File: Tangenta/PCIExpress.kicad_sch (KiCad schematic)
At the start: 0 parts

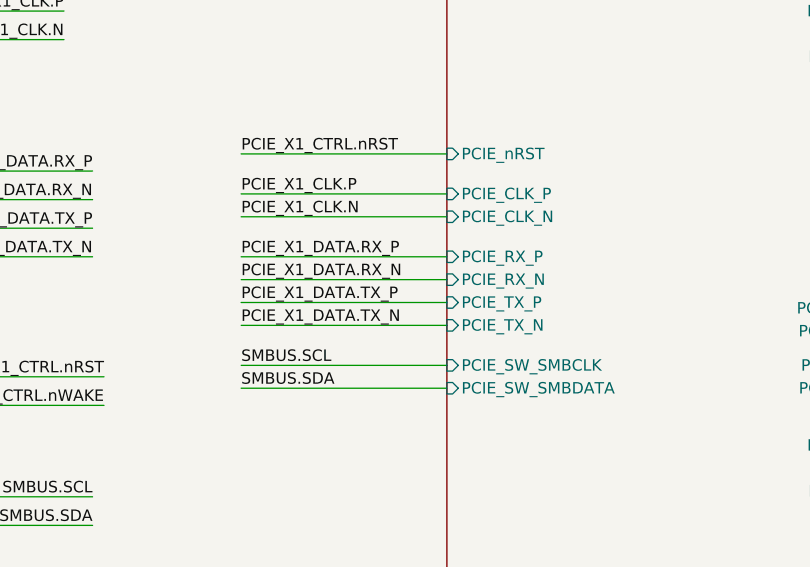
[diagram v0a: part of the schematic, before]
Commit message: PCIe fix in progress...
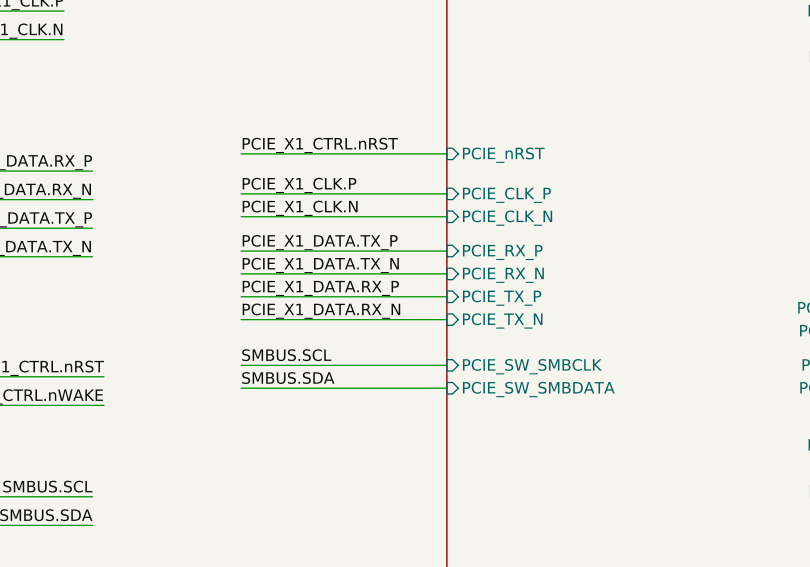
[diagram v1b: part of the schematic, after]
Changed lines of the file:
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@@
 	(wire
 		(pts
-			(xy 101.6 120.015) (xy 124.46 120.015)
+			(xy 101.6 119.38) (xy 124.46 119.38)
 		)
 		(stroke
@@
 	(wire
 		(pts
-			(xy 101.6 117.475) (xy 124.46 117.475)
+			(xy 101.6 116.84) (xy 124.46 116.84)
 		)
 		(stroke
@@
 	(wire
 		(pts
-			(xy 101.6 125.095) (xy 124.46 125.095)
+			(xy 101.6 124.46) (xy 124.46 124.46)
 		)
 		(stroke
@@
 	(wire
 		(pts
-			(xy 101.6 122.555) (xy 124.46 122.555)
+			(xy 101.6 121.92) (xy 124.46 121.92)
 		)
 		(stroke
@@
 	)
 	(label "PCIE_X1_DATA.TX_P"
-		(at 101.6 122.555 0)
+		(at 101.6 116.84 0)
 		(effects
 			(font
@@
 	)
 	(label "PCIE_X1_DATA.TX_N"
-		(at 101.6 125.095 0)
+		(at 101.6 119.38 0)
 		(effects
 			(font
@@
 	)
 	(label "PCIE_X1_DATA.RX_P"
-		(at 101.6 117.475 0)
+		(at 101.6 121.92 0)
 		(effects
 			(font
@@
 	)
 	(label "PCIE_X1_DATA.RX_N"
-		(at 101.6 120.015 0)
+		(at 101.6 124.46 0)
 		(effects
 			(font
@@
 		)
 		(pin "PCIE_RX_P" input
-			(at 124.46 117.475 180)
+			(at 124.46 116.84 180)
 			(effects
 				(font
@@
 		)
 		(pin "PCIE_TX_P" input
-			(at 124.46 122.555 180)
+			(at 124.46 121.92 180)
 			(effects
 				(font
@@
 		)
 		(pin "PCIE_TX_N" input
-			(at 124.46 125.095 180)
+			(at 124.46 124.46 180)
 			(effects
 				(font
@@
 		)
 		(pin "PCIE_RX_N" input
-			(at 124.46 120.015 180)
+			(at 124.46 119.38 180)
 			(effects
 				(font
